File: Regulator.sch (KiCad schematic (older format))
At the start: 6 parts, among them P5 CONN_01X02, U3 LM1084IS-3.3/NOPB

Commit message: Began layout of board
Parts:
- added C13, C7: 10uF, symbol C
- added D5: LED, symbol LED
- added R6: 270, symbol R
- added U4: LM1084IS-5.0/NOPB, TO-263, symbol LM1084IS-5.0/NOPB
- gave numbers to parts that had none: 2
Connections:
- net GND: now also C13.2, C7.2, D5.2 (K), U4.1 (GND)
- net Vbatt: now also C7.1, U4.3 (IN)
- new net: D5.1 (A), R6.1
- new net +5V: C13.1, R6.2, U4.2 (OUT)
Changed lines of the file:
@@
 LIBS:xbee
 LIBS:avbay-cache
-EELAYER 25 0
+EELAYER 27 0
 EELAYER END
 $Descr A4 11693 8268
@@
 Sheet 3 3
 Title ""
-Date ""
+Date "20 oct 2014"
 Rev ""
 Comp ""
@@
 $EndDescr
 $Comp
-L 3V3 #PWR25
+L 3V3 #PWR028
 U 1 1 543769E5
 P 2300 2050
-F 0 "#PWR25" H 2300 2150 40  0001 C CNN
+F 0 "#PWR028" H 2300 2150 40  0001 C CNN
 F 1 "3V3" H 2300 2175 40  0000 C CNN
 F 2 "" H 2300 2050 60  0000 C CNN
@@
 Wire Wire Line
 	2300 2150 2300 2050
-Text HLabel 1050 2150 0    60   Input ~ 0
+Text HLabel 800  2150 0    60   Input ~ 0
 Vbatt
 Wire Wire Line
-	1250 2150 1050 2150
-$Comp
-L GND #PWR24
+	800  2150 1250 2150
+$Comp
+L GND #PWR029
 U 1 1 54376AC4
 P 1650 2650
-F 0 "#PWR24" H 1650 2650 30  0001 C CNN
+F 0 "#PWR029" H 1650 2650 30  0001 C CNN
 F 1 "GND" H 1650 2580 30  0001 C CNN
 F 2 "" H 1650 2650 60  0000 C CNN
@@
 	1200 1550 1200 1700
 $Comp
-L GND #PWR23
+L GND #PWR030
 U 1 1 54376D30
 P 1200 1700
-F 0 "#PWR23" H 1200 1700 30  0001 C CNN
+F 0 "#PWR030" H 1200 1700 30  0001 C CNN
 F 1 "GND" H 1200 1630 30  0001 C CNN
 F 2 "" H 1200 1700 60  0000 C CNN
@@
 $EndComp
 $Comp
-L LED D?
+L LED D6
 U 1 1 543780B4
 P 3050 2550
-F 0 "D?" H 3050 2650 50  0000 C CNN
+F 0 "D6" H 3050 2650 50  0000 C CNN
 F 1 "LED" H 3050 2450 50  0000 C CNN
 F 2 "" H 3050 2550 60  0000 C CNN
@@
 $EndComp
 $Comp
-L R R?
+L R R7
 U 1 1 5437812D
 P 2700 2150
-F 0 "R?" V 2780 2150 40  0000 C CNN
+F 0 "R7" H 2780 2150 40  0000 C CNN
 F 1 "48" V 2707 2151 40  0000 C CNN
 F 2 "" V 2630 2150 30  0000 C CNN
@@
 	1850 2750 3050 2750
 Connection ~ 1850 2700
+$Comp
+L LM1084IS-5.0/NOPB U4
+U 1 1 5444771F
+P 1650 3450
+F 0 "U4" H 1850 3250 40  0000 C CNN
+F 1 "LM1084IS-5.0/NOPB" H 1350 3650 40  0000 L CNN
+F 2 "TO-263" H 1650 3550 30  0000 C CIN
+F 3 "~" H 1650 3450 60  0000 C CNN
+	1    1650 3450
+	1    0    0    -1
+$EndComp
+Wire Wire Line
+	1250 3400 900  3400
+Wire Wire Line
+	900  3400 900  2150
+Connection ~ 900  2150
+$Comp
+L C C7
+U 1 1 5444778F
+P 1150 3750
+F 0 "C7" H 1150 3850 40  0000 L CNN
+F 1 "10uF" H 1156 3665 40  0000 L CNN
+F 2 "" H 1188 3600 30  0000 C CNN
+F 3 "" H 1150 3750 60  0000 C CNN
+	1    1150 3750
+	1    0    0    -1
+$EndComp
+Connection ~ 1150 3400
+Wire Wire Line
+	1150 3400 1150 3550
+$Comp
+L GND #PWR031
+U 1 1 544477E3
+P 1650 4050
+F 0 "#PWR031" H 1650 4050 30  0001 C CNN
+F 1 "GND" H 1650 3980 30  0001 C CNN
+F 2 "" H 1650 4050 60  0000 C CNN
+F 3 "" H 1650 4050 60  0000 C CNN
+	1    1650 4050
+	1    0    0    -1
+$EndComp
+Wire Wire Line
+	1150 4000 1150 3950
+Wire Wire Line
+	1650 3700 1650 4050
+Wire Wire Line
+	1150 4000 2700 4000
+Connection ~ 1650 4000
+$Comp
+L C C13
+U 1 1 5444789E
+P 2100 3750
+F 0 "C13" H 2100 3850 40  0000 L CNN
+F 1 "10uF" H 2106 3665 40  0000 L CNN
+F 2 "" H 2138 3600 30  0000 C CNN
+F 3 "" H 2100 3750 60  0000 C CNN
+	1    2100 3750
+	1    0    0    -1
+$EndComp
+Wire Wire Line
+	2050 3400 2150 3400
+Wire Wire Line
+	2100 3300 2100 3550
+Wire Wire Line
+	2100 4000 2100 3950
+$Comp
+L LED D5
+U 1 1 544478E6
+P 2700 3750
+F 0 "D5" H 2700 3850 50  0000 C CNN
+F 1 "LED" H 2700 3650 50  0000 C CNN
+F 2 "" H 2700 3750 60  0000 C CNN
+F 3 "" H 2700 3750 60  0000 C CNN
+	1    2700 3750
+	0    1    1    0
+$EndComp
+$Comp
+L R R6
+U 1 1 544478F1
+P 2400 3400
+F 0 "R6" H 2480 3400 40  0000 C CNN
+F 1 "270" V 2407 3401 40  0000 C CNN
+F 2 "" V 2330 3400 30  0000 C CNN
+F 3 "" H 2400 3400 30  0000 C CNN
+	1    2400 3400
+	0    1    1    0
+$EndComp
+Connection ~ 2100 3400
+Wire Wire Line
+	2650 3400 2700 3400
+Wire Wire Line
+	2700 3400 2700 3550
+Wire Wire Line
+	2700 4000 2700 3950
+Connection ~ 2100 4000
+$Comp
+L +5V #PWR032
+U 1 1 544485F5
+P 2100 3300
+F 0 "#PWR032" H 2100 3390 20  0001 C CNN
+F 1 "+5V" H 2100 3390 30  0000 C CNN
+F 2 "" H 2100 3300 60  0000 C CNN
+F 3 "" H 2100 3300 60  0000 C CNN
+	1    2100 3300
+	1    0    0    -1
+$EndComp
 $EndSCHEMATC

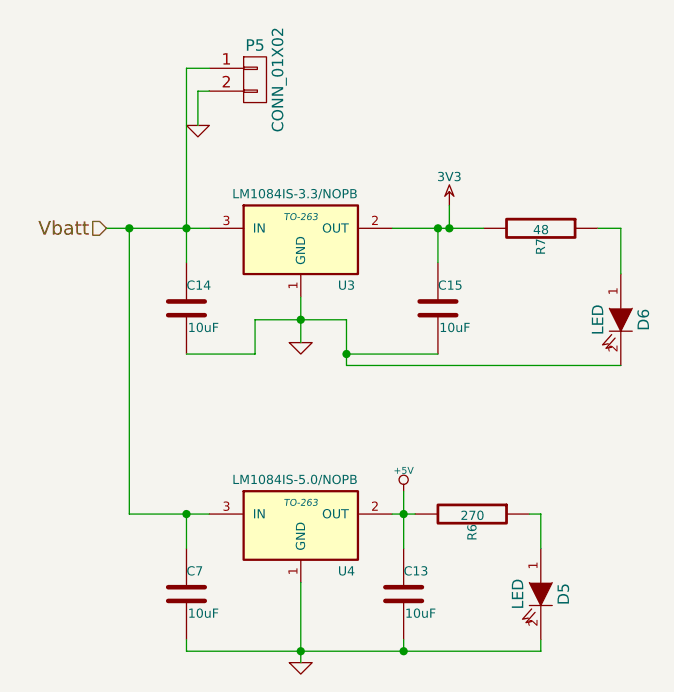
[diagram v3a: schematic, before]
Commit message: Added pyro circuits
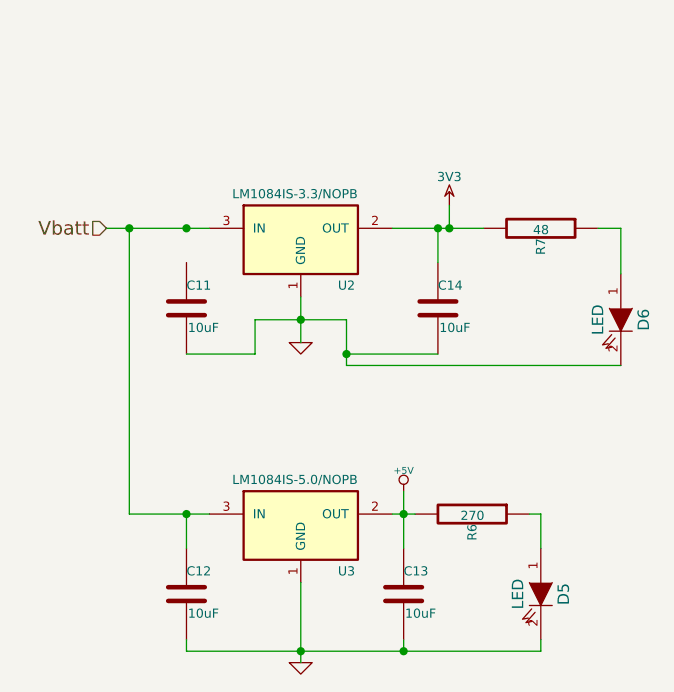
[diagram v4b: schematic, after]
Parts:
- removed P5: CONN_01X02, symbol CONN_01X02
- C11: renamed from C14; footprint (none) -> Capacitors_SMD:C_0805_HandSoldering
- C12: renamed from C7; footprint (none) -> Capacitors_SMD:C_0805_HandSoldering
- C13: footprint (none) -> Capacitors_SMD:C_0805_HandSoldering
- C14: renamed from C15; footprint (none) -> Capacitors_SMD:C_0805_HandSoldering
- D5, D6: footprint (none) -> LEDs:LED-0805
- R6, R7: footprint (none) -> Resistors_SMD:R_0805_HandSoldering
- U2: renamed from U3; footprint TO-263 -> (none)
- U3: renamed from U4; footprint TO-263 -> (none)
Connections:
- net Vbatt: no longer C11.1
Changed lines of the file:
@@
 LIBS:xbee
 LIBS:avbay-cache
-EELAYER 27 0
+EELAYER 25 0
 EELAYER END
 $Descr A4 11693 8268
@@
 $EndComp
 $Comp
-L LM1084IS-3.3/NOPB U3
+L LM1084IS-3.3/NOPB U2
 U 1 1 543769F9
 P 1650 2200
-F 0 "U3" H 1850 2000 40  0000 C CNN
+F 0 "U2" H 1850 2000 40  0000 C CNN
 F 1 "LM1084IS-3.3/NOPB" H 1350 2400 40  0000 L CNN
-F 2 "TO-263" H 1650 2300 30  0000 C CIN
+F 2 "" H 1650 2300 30  0001 C CIN
 F 3 "" H 1650 2200 60  0000 C CNN
 	1    1650 2200
@@
 $EndComp
 $Comp
-L C C15
+L C C14
 U 1 1 54376AE8
 P 2250 2500
-F 0 "C15" H 2250 2600 40  0000 L CNN
+F 0 "C14" H 2250 2600 40  0000 L CNN
 F 1 "10uF" H 2256 2415 40  0000 L CNN
-F 2 "" H 2288 2350 30  0000 C CNN
+F 2 "Capacitors_SMD:C_0805_HandSoldering" H 2288 2350 30  0001 C CNN
 F 3 "" H 2250 2500 60  0000 C CNN
 	1    2250 2500
@@
 $EndComp
 $Comp
-L C C14
+L C C11
 U 1 1 54376B1F
 P 1150 2500
-F 0 "C14" H 1150 2600 40  0000 L CNN
+F 0 "C11" H 1150 2600 40  0000 L CNN
 F 1 "10uF" H 1156 2415 40  0000 L CNN
-F 2 "" H 1188 2350 30  0000 C CNN
+F 2 "Capacitors_SMD:C_0805_HandSoldering" H 1188 2350 30  0001 C CNN
 F 3 "" H 1150 2500 60  0000 C CNN
 	1    1150 2500
@@
 F 0 "D6" H 3050 2650 50  0000 C CNN
 F 1 "LED" H 3050 2450 50  0000 C CNN
-F 2 "" H 3050 2550 60  0000 C CNN
+F 2 "LEDs:LED-0805" H 3050 2550 60  0001 C CNN
 F 3 "" H 3050 2550 60  0000 C CNN
 	1    3050 2550
@@
 F 0 "R7" H 2780 2150 40  0000 C CNN
 F 1 "48" V 2707 2151 40  0000 C CNN
-F 2 "" V 2630 2150 30  0000 C CNN
+F 2 "Resistors_SMD:R_0805_HandSoldering" V 2630 2150 30  0001 C CNN
 F 3 "" H 2700 2150 30  0000 C CNN
 	1    2700 2150
@@
 $EndComp
 $Comp
-L LM1084IS-5.0/NOPB U4
+L LM1084IS-5.0/NOPB U3
 U 1 1 5444771F
 P 1650 3450
-F 0 "U4" H 1850 3250 40  0000 C CNN
+F 0 "U3" H 1850 3250 40  0000 C CNN
 F 1 "LM1084IS-5.0/NOPB" H 1350 3650 40  0000 L CNN
-F 2 "TO-263" H 1650 3550 30  0000 C CIN
+F 2 "" H 1650 3550 30  0001 C CIN
 F 3 "~" H 1650 3450 60  0000 C CNN
 	1    1650 3450
@@
 $EndComp
 $Comp
-L C C7
+L C C12
 U 1 1 5444778F
 P 1150 3750
-F 0 "C7" H 1150 3850 40  0000 L CNN
+F 0 "C12" H 1150 3850 40  0000 L CNN
 F 1 "10uF" H 1156 3665 40  0000 L CNN
-F 2 "" H 1188 3600 30  0000 C CNN
+F 2 "Capacitors_SMD:C_0805_HandSoldering" H 1188 3600 30  0001 C CNN
 F 3 "" H 1150 3750 60  0000 C CNN
 	1    1150 3750
@@
 $EndComp
 $Comp
-L GND #PWR029
+L GND #PWR028
 U 1 1 544477E3
 P 1650 4050
-F 0 "#PWR029" H 1650 4050 30  0001 C CNN
+F 0 "#PWR028" H 1650 4050 30  0001 C CNN
 F 1 "GND" H 1650 3980 30  0001 C CNN
 F 2 "" H 1650 4050 60  0000 C CNN
@@
 F 0 "C13" H 2100 3850 40  0000 L CNN
 F 1 "10uF" H 2106 3665 40  0000 L CNN
-F 2 "" H 2138 3600 30  0000 C CNN
+F 2 "Capacitors_SMD:C_0805_HandSoldering" H 2138 3600 30  0001 C CNN
 F 3 "" H 2100 3750 60  0000 C CNN
 	1    2100 3750
@@
 F 0 "D5" H 2700 3850 50  0000 C CNN
 F 1 "LED" H 2700 3650 50  0000 C CNN
-F 2 "" H 2700 3750 60  0000 C CNN
+F 2 "LEDs:LED-0805" H 2700 3750 60  0001 C CNN
 F 3 "" H 2700 3750 60  0000 C CNN
 	1    2700 3750
@@
 F 0 "R6" H 2480 3400 40  0000 C CNN
 F 1 "270" V 2407 3401 40  0000 C CNN
-F 2 "" V 2330 3400 30  0000 C CNN
+F 2 "Resistors_SMD:R_0805_HandSoldering" V 2330 3400 30  0001 C CNN
 F 3 "" H 2400 3400 30  0000 C CNN
 	1    2400 3400
@@
 $EndComp
 $Comp
-L +5V #PWR030
+L +5V #PWR029
 U 1 1 544485F5
 P 2100 3300
-F 0 "#PWR030" H 2100 3390 20  0001 C CNN
+F 0 "#PWR029" H 2100 3390 20  0001 C CNN
 F 1 "+5V" H 2100 3390 30  0000 C CNN
 F 2 "" H 2100 3300 60  0000 C CNN
@@
 	2700 4000 2700 3950
 Connection ~ 2100 4000
-$Comp
-L GND #PWR028
-U 1 1 54376D30
-P 1200 1700
-F 0 "#PWR028" H 1200 1700 30  0001 C CNN
-F 1 "GND" H 1200 1630 30  0001 C CNN
-F 2 "" H 1200 1700 60  0000 C CNN
-F 3 "" H 1200 1700 60  0000 C CNN
-	1    1200 1700
-	1    0    0    -1
-$EndComp
-Wire Wire Line
-	1250 1450 1150 1450
-Wire Wire Line
-	1250 1550 1200 1550
-Wire Wire Line
-	1200 1550 1200 1700
-$Comp
-L CONN_01X02 P5
-U 1 1 54376C6D
-P 1450 1500
-F 0 "P5" H 1450 1650 50  0000 C CNN
-F 1 "CONN_01X02" V 1550 1500 50  0000 C CNN
-F 2 "" H 1450 1500 60  0000 C CNN
-F 3 "" H 1450 1500 60  0000 C CNN
-	1    1450 1500
-	1    0    0    -1
-$EndComp
-Wire Wire Line
-	1150 1450 1150 2300
 $EndSCHEMATC

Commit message: Began laying out PCB
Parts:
- U2, U3: footprint (none) -> SMD_Packages:DPAK-3
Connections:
- net Vbatt: now also C11.1
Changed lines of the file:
@@
 F 0 "U2" H 1850 2000 40  0000 C CNN
 F 1 "LM1084IS-3.3/NOPB" H 1350 2400 40  0000 L CNN
-F 2 "" H 1650 2300 30  0001 C CIN
+F 2 "SMD_Packages:DPAK-3" H 1650 2300 30  0001 C CIN
 F 3 "" H 1650 2200 60  0000 C CNN
 	1    1650 2200
@@
 F 0 "U3" H 1850 3250 40  0000 C CNN
 F 1 "LM1084IS-5.0/NOPB" H 1350 3650 40  0000 L CNN
-F 2 "" H 1650 3550 30  0001 C CIN
+F 2 "SMD_Packages:DPAK-3" H 1650 3550 30  0001 C CIN
 F 3 "~" H 1650 3450 60  0000 C CNN
 	1    1650 3450
@@
 	2700 4000 2700 3950
 Connection ~ 2100 4000
+Wire Wire Line
+	1150 2150 1150 2300
 $EndSCHEMATC

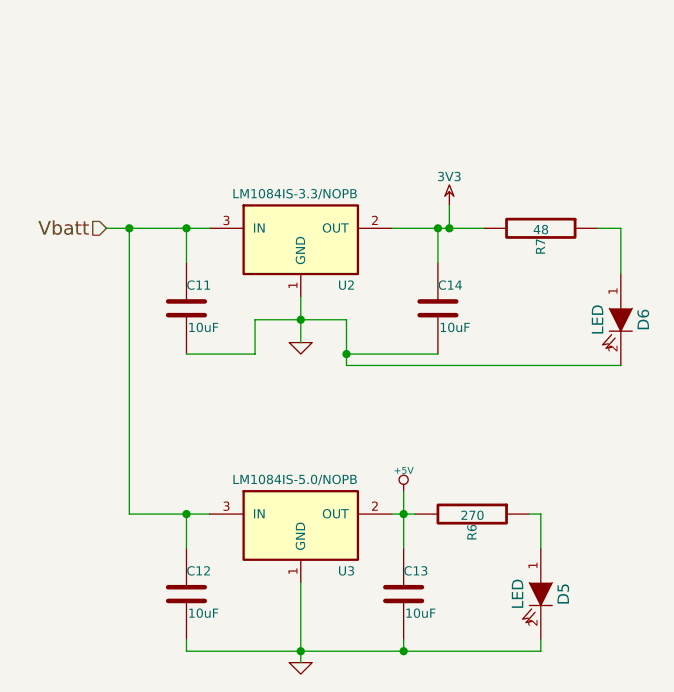
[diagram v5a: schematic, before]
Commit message: New MOSFETs
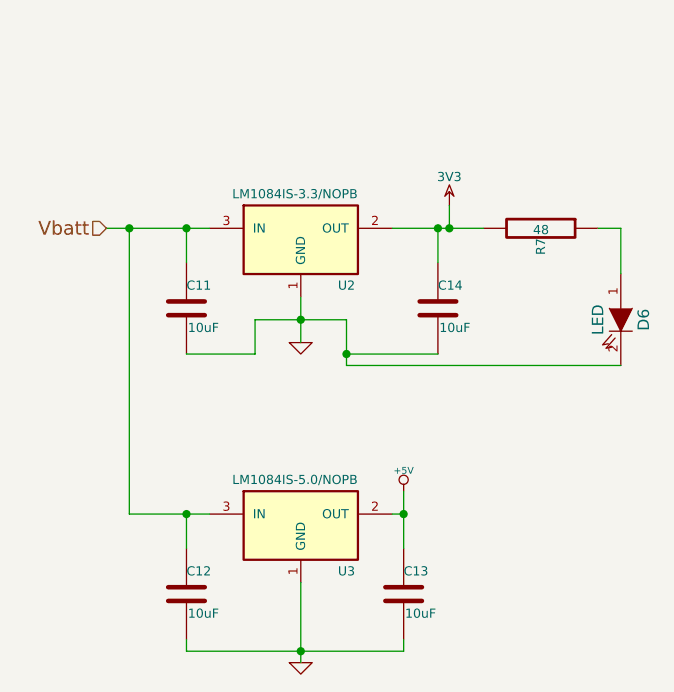
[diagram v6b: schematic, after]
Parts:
- removed D5: LED, LEDs:LED-0805, symbol LED
- removed R6: 270, Resistors_SMD:R_0805_HandSoldering, symbol R
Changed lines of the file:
@@
 LIBS:xbee
 LIBS:avbay-cache
-EELAYER 25 0
+EELAYER 27 0
 EELAYER END
 $Descr A4 11693 8268
@@
 Sheet 3 4
 Title ""
-Date "4 dec 2014"
+Date "6 dec 2014"
 Rev ""
 Comp ""
@@
 $EndDescr
 $Comp
-L 3V3 #PWR026
+L 3V3 #PWR29
 U 1 1 543769E5
 P 2300 2050
-F 0 "#PWR026" H 2300 2150 40  0001 C CNN
+F 0 "#PWR29" H 2300 2150 40  0001 C CNN
 F 1 "3V3" H 2300 2175 40  0000 C CNN
 F 2 "" H 2300 2050 60  0000 C CNN
@@
 Vbatt
 $Comp
-L GND #PWR027
+L GND #PWR26
 U 1 1 54376AC4
 P 1650 2650
-F 0 "#PWR027" H 1650 2650 30  0001 C CNN
+F 0 "#PWR26" H 1650 2650 30  0001 C CNN
 F 1 "GND" H 1650 2580 30  0001 C CNN
 F 2 "" H 1650 2650 60  0000 C CNN
@@
 $EndComp
 $Comp
-L GND #PWR028
+L GND #PWR27
 U 1 1 544477E3
 P 1650 4050
-F 0 "#PWR028" H 1650 4050 30  0001 C CNN
+F 0 "#PWR27" H 1650 4050 30  0001 C CNN
 F 1 "GND" H 1650 3980 30  0001 C CNN
 F 2 "" H 1650 4050 60  0000 C CNN
@@
 $EndComp
 $Comp
-L LED D5
-U 1 1 544478E6
-P 2700 3750
-F 0 "D5" H 2700 3850 50  0000 C CNN
-F 1 "LED" H 2700 3650 50  0000 C CNN
-F 2 "LEDs:LED-0805" H 2700 3750 60  0001 C CNN
-F 3 "" H 2700 3750 60  0000 C CNN
-	1    2700 3750
-	0    1    1    0
-$EndComp
-$Comp
-L R R6
-U 1 1 544478F1
-P 2400 3400
-F 0 "R6" H 2480 3400 40  0000 C CNN
-F 1 "270" V 2407 3401 40  0000 C CNN
-F 2 "Resistors_SMD:R_0805_HandSoldering" V 2330 3400 30  0001 C CNN
-F 3 "" H 2400 3400 30  0000 C CNN
-	1    2400 3400
-	0    1    1    0
-$EndComp
-$Comp
-L +5V #PWR029
+L +5V #PWR28
 U 1 1 544485F5
 P 2100 3300
-F 0 "#PWR029" H 2100 3390 20  0001 C CNN
+F 0 "#PWR28" H 2100 3390 20  0001 C CNN
 F 1 "+5V" H 2100 3390 30  0000 C CNN
 F 2 "" H 2100 3300 60  0000 C CNN
@@
 Connection ~ 1850 2700
 Wire Wire Line
-	1250 3400 900  3400
+	900  3400 1250 3400
 Wire Wire Line
 	900  3400 900  2150
@@
 Wire Wire Line
 	1650 3700 1650 4050
-Wire Wire Line
-	1150 4000 2700 4000
 Connection ~ 1650 4000
 Wire Wire Line
-	2050 3400 2150 3400
-Wire Wire Line
 	2100 3300 2100 3550
+Connection ~ 2100 3400
+Wire Wire Line
+	1150 2150 1150 2300
+Wire Wire Line
+	1150 4000 2100 4000
 Wire Wire Line
 	2100 4000 2100 3950
-Connection ~ 2100 3400
-Wire Wire Line
-	2650 3400 2700 3400
-Wire Wire Line
-	2700 3400 2700 3550
-Wire Wire Line
-	2700 4000 2700 3950
-Connection ~ 2100 4000
-Wire Wire Line
-	1150 2150 1150 2300
+Wire Wire Line
+	2100 3400 2050 3400
 $EndSCHEMATC
